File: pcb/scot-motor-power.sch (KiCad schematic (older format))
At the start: 16 parts, among them U6 TSR_1-2465, U7 INA260, U8 MCP1703A-3302_SOT223, U9 MCP1703A-5002_SOT223

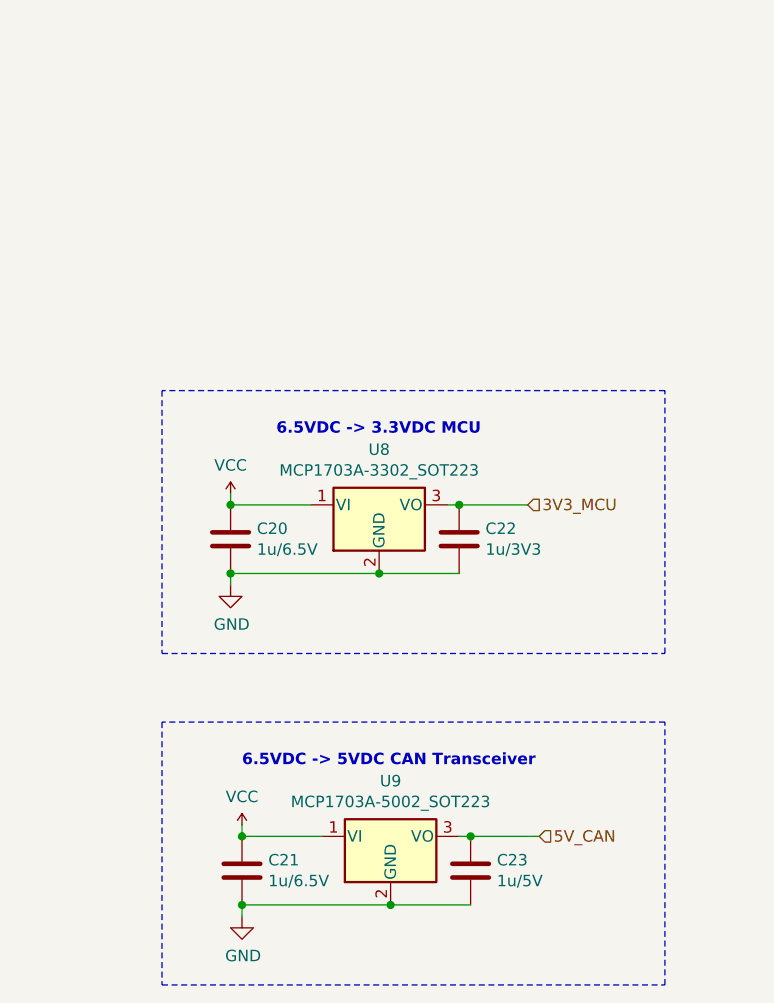
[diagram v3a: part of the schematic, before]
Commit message: pcb: Link brake clutch to e-stop, aesthetic tweaks.
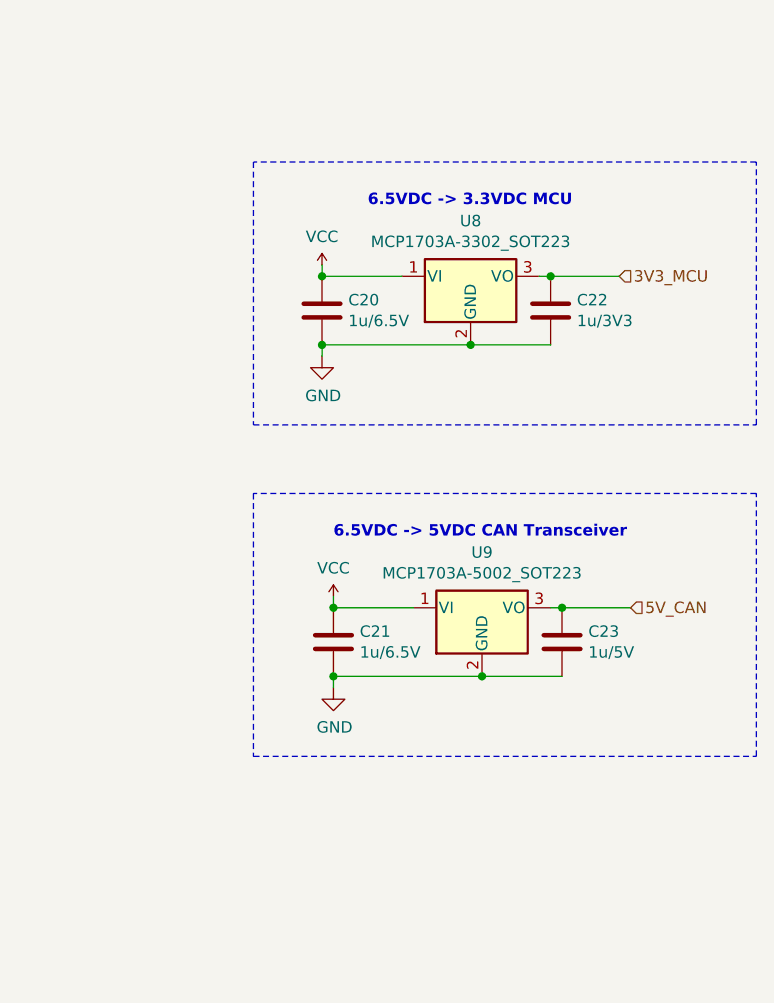
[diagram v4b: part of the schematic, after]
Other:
- moved on the sheet: C20, C21, C22, C23, U8, U9
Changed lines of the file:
@@
 L Regulator_Linear:MCP1703A-3302_SOT223 U8
 U 1 1 5F0E873C
-P 8450 4300
-F 0 "U8" H 8450 4542 50  0000 C CNN
-F 1 "MCP1703A-3302_SOT223" H 8450 4451 50  0000 C CNN
-F 2 "Package_TO_SOT_SMD:SOT-223-3_TabPin2" H 8450 4500 50  0001 C CNN
-F 3 "http://ww1.microchip.com/downloads/en/DeviceDoc/20005122B.pdf" H 8450 4250 50  0001 C CNN
-	1    8450 4300
+P 8850 3300
+F 0 "U8" H 8850 3542 50  0000 C CNN
+F 1 "MCP1703A-3302_SOT223" H 8850 3451 50  0000 C CNN
+F 2 "Package_TO_SOT_SMD:SOT-223-3_TabPin2" H 8850 3500 50  0001 C CNN
+F 3 "http://ww1.microchip.com/downloads/en/DeviceDoc/20005122B.pdf" H 8850 3250 50  0001 C CNN
+	1    8850 3300
 	1    0    0    -1
 $EndComp
@@
 L Device:C C20
 U 1 1 5F0E8CBD
-P 7800 4450
-F 0 "C20" H 7915 4496 50  0000 L CNN
-F 1 "1u/6.5V" H 7915 4405 50  0000 L CNN
-F 2 "Capacitor_SMD:C_0603_1608Metric_Pad1.05x0.95mm_HandSolder" H 7838 4300 50  0001 C CNN
-F 3 "~" H 7800 4450 50  0001 C CNN
-	1    7800 4450
-	1    0    0    -1
-$EndComp
-Wire Wire Line
-	8450 4600 7800 4600
-Wire Wire Line
-	7800 4300 8150 4300
+P 8200 3450
+F 0 "C20" H 8315 3496 50  0000 L CNN
+F 1 "1u/6.5V" H 8315 3405 50  0000 L CNN
+F 2 "Capacitor_SMD:C_0603_1608Metric_Pad1.05x0.95mm_HandSolder" H 8238 3300 50  0001 C CNN
+F 3 "~" H 8200 3450 50  0001 C CNN
+	1    8200 3450
+	1    0    0    -1
+$EndComp
+Wire Wire Line
+	8850 3600 8200 3600
+Wire Wire Line
+	8200 3300 8550 3300
 $Comp
 L Device:C C22
 U 1 1 5F0E9FCA
-P 8800 4450
-F 0 "C22" H 8915 4496 50  0000 L CNN
-F 1 "1u/3V3" H 8915 4405 50  0000 L CNN
-F 2 "Capacitor_SMD:C_0603_1608Metric_Pad1.05x0.95mm_HandSolder" H 8838 4300 50  0001 C CNN
-F 3 "~" H 8800 4450 50  0001 C CNN
-	1    8800 4450
-	1    0    0    -1
-$EndComp
-Wire Wire Line
-	8450 4600 8800 4600
-Connection ~ 8450 4600
-Wire Wire Line
-	8800 4300 8750 4300
+P 9200 3450
+F 0 "C22" H 9315 3496 50  0000 L CNN
+F 1 "1u/3V3" H 9315 3405 50  0000 L CNN
+F 2 "Capacitor_SMD:C_0603_1608Metric_Pad1.05x0.95mm_HandSolder" H 9238 3300 50  0001 C CNN
+F 3 "~" H 9200 3450 50  0001 C CNN
+	1    9200 3450
+	1    0    0    -1
+$EndComp
+Wire Wire Line
+	8850 3600 9200 3600
+Connection ~ 8850 3600
+Wire Wire Line
+	9200 3300 9150 3300
 Wire Wire Line
 	5350 5100 5200 5100
@@
 L agg-kicad:VCC #PWR0130
 U 1 1 5F0ED075
-P 7800 4250
-F 0 "#PWR0130" H 7800 4360 50  0001 L CNN
-F 1 "VCC" H 7800 4373 50  0000 C CNN
-F 2 "" H 7800 4250 50  0001 C CNN
-F 3 "" H 7800 4250 50  0001 C CNN
-	1    7800 4250
+P 8200 3250
+F 0 "#PWR0130" H 8200 3360 50  0001 L CNN
+F 1 "VCC" H 8200 3373 50  0000 C CNN
+F 2 "" H 8200 3250 50  0001 C CNN
+F 3 "" H 8200 3250 50  0001 C CNN
+	1    8200 3250
 	1    0    0    -1
 $EndComp
@@
 L power:GND #PWR0131
 U 1 1 5F0ED86E
-P 7800 4650
-F 0 "#PWR0131" H 7800 4400 50  0001 C CNN
-F 1 "GND" H 7805 4477 50  0000 C CNN
-F 2 "" H 7800 4650 50  0001 C CNN
-F 3 "" H 7800 4650 50  0001 C CNN
-	1    7800 4650
-	1    0    0    -1
-$EndComp
-Wire Wire Line
-	7800 4600 7800 4650
-Connection ~ 7800 4600
-Wire Wire Line
-	7800 4300 7800 4250
-Connection ~ 7800 4300
+P 8200 3650
+F 0 "#PWR0131" H 8200 3400 50  0001 C CNN
+F 1 "GND" H 8205 3477 50  0000 C CNN
+F 2 "" H 8200 3650 50  0001 C CNN
+F 3 "" H 8200 3650 50  0001 C CNN
+	1    8200 3650
+	1    0    0    -1
+$EndComp
+Wire Wire Line
+	8200 3600 8200 3650
+Connection ~ 8200 3600
+Wire Wire Line
+	8200 3300 8200 3250
+Connection ~ 8200 3300
 $Comp
 L agg-kicad:VCC #PWR0132
@@
 	1    0    0    -1
 $EndComp
-Text HLabel 9100 4300 2    50   Input ~ 0
+Text HLabel 9500 3300 2    50   Input ~ 0
 3V3_MCU
 Wire Wire Line
-	9100 4300 8800 4300
-Connection ~ 8800 4300
+	9500 3300 9200 3300
+Connection ~ 9200 3300
 $Comp
 L Device:C C21
 U 1 1 5F111717
-P 7850 5900
-F 0 "C21" H 7965 5946 50  0000 L CNN
-F 1 "1u/6.5V" H 7965 5855 50  0000 L CNN
-F 2 "Capacitor_SMD:C_0603_1608Metric_Pad1.05x0.95mm_HandSolder" H 7888 5750 50  0001 C CNN
-F 3 "~" H 7850 5900 50  0001 C CNN
-	1    7850 5900
-	1    0    0    -1
-$EndComp
-Wire Wire Line
-	7850 5750 8200 5750
+P 8250 4900
+F 0 "C21" H 8365 4946 50  0000 L CNN
+F 1 "1u/6.5V" H 8365 4855 50  0000 L CNN
+F 2 "Capacitor_SMD:C_0603_1608Metric_Pad1.05x0.95mm_HandSolder" H 8288 4750 50  0001 C CNN
+F 3 "~" H 8250 4900 50  0001 C CNN
+	1    8250 4900
+	1    0    0    -1
+$EndComp
+Wire Wire Line
+	8250 4750 8600 4750
 $Comp
 L Device:C C23
 U 1 1 5F111723
-P 8850 5900
-F 0 "C23" H 8965 5946 50  0000 L CNN
-F 1 "1u/5V" H 8965 5855 50  0000 L CNN
-F 2 "Capacitor_SMD:C_0603_1608Metric_Pad1.05x0.95mm_HandSolder" H 8888 5750 50  0001 C CNN
-F 3 "~" H 8850 5900 50  0001 C CNN
-	1    8850 5900
-	1    0    0    -1
-$EndComp
-Wire Wire Line
-	8850 5750 8800 5750
+P 9250 4900
+F 0 "C23" H 9365 4946 50  0000 L CNN
+F 1 "1u/5V" H 9365 4855 50  0000 L CNN
+F 2 "Capacitor_SMD:C_0603_1608Metric_Pad1.05x0.95mm_HandSolder" H 9288 4750 50  0001 C CNN
+F 3 "~" H 9250 4900 50  0001 C CNN
+	1    9250 4900
+	1    0    0    -1
+$EndComp
+Wire Wire Line
+	9250 4750 9200 4750
 $Comp
 L agg-kicad:VCC #PWR0134
 U 1 1 5F111730
-P 7850 5700
-F 0 "#PWR0134" H 7850 5810 50  0001 L CNN
-F 1 "VCC" H 7850 5823 50  0000 C CNN
-F 2 "" H 7850 5700 50  0001 C CNN
-F 3 "" H 7850 5700 50  0001 C CNN
-	1    7850 5700
+P 8250 4700
+F 0 "#PWR0134" H 8250 4810 50  0001 L CNN
+F 1 "VCC" H 8250 4823 50  0000 C CNN
+F 2 "" H 8250 4700 50  0001 C CNN
+F 3 "" H 8250 4700 50  0001 C CNN
+	1    8250 4700
 	1    0    0    -1
 $EndComp
@@
 L power:GND #PWR0135
 U 1 1 5F11173A
-P 7850 6100
-F 0 "#PWR0135" H 7850 5850 50  0001 C CNN
-F 1 "GND" H 7855 5927 50  0000 C CNN
-F 2 "" H 7850 6100 50  0001 C CNN
-F 3 "" H 7850 6100 50  0001 C CNN
-	1    7850 6100
-	1    0    0    -1
-$EndComp
-Wire Wire Line
-	7850 6050 7850 6100
-Connection ~ 7850 6050
-Wire Wire Line
-	7850 5750 7850 5700
-Connection ~ 7850 5750
-Text HLabel 9150 5750 2    50   Input ~ 0
+P 8250 5100
+F 0 "#PWR0135" H 8250 4850 50  0001 C CNN
+F 1 "GND" H 8255 4927 50  0000 C CNN
+F 2 "" H 8250 5100 50  0001 C CNN
+F 3 "" H 8250 5100 50  0001 C CNN
+	1    8250 5100
+	1    0    0    -1
+$EndComp
+Wire Wire Line
+	8250 5050 8250 5100
+Connection ~ 8250 5050
+Wire Wire Line
+	8250 4750 8250 4700
+Connection ~ 8250 4750
+Text HLabel 9550 4750 2    50   Input ~ 0
 5V_CAN
 Wire Wire Line
-	9150 5750 8850 5750
-Connection ~ 8850 5750
-Wire Wire Line
-	7850 6050 8500 6050
+	9550 4750 9250 4750
+Connection ~ 9250 4750
+Wire Wire Line
+	8250 5050 8900 5050
 $Comp
 L Regulator_Linear:MCP1703A-5002_SOT223 U9
 U 1 1 5F1147A2
-P 8500 5750
-F 0 "U9" H 8500 5992 50  0000 C CNN
-F 1 "MCP1703A-5002_SOT223" H 8500 5901 50  0000 C CNN
-F 2 "Package_TO_SOT_SMD:SOT-223-3_TabPin2" H 8500 5950 50  0001 C CNN
-F 3 "http://ww1.microchip.com/downloads/en/DeviceDoc/20005122B.pdf" H 8500 5700 50  0001 C CNN
-	1    8500 5750
-	1    0    0    -1
-$EndComp
-Connection ~ 8500 6050
-Wire Wire Line
-	8500 6050 8850 6050
+P 8900 4750
+F 0 "U9" H 8900 4992 50  0000 C CNN
+F 1 "MCP1703A-5002_SOT223" H 8900 4901 50  0000 C CNN
+F 2 "Package_TO_SOT_SMD:SOT-223-3_TabPin2" H 8900 4950 50  0001 C CNN
+F 3 "http://ww1.microchip.com/downloads/en/DeviceDoc/20005122B.pdf" H 8900 4700 50  0001 C CNN
+	1    8900 4750
+	1    0    0    -1
+$EndComp
+Connection ~ 8900 5050
+Wire Wire Line
+	8900 5050 9250 5050
 $Comp
 L Regulator_Switching:TSR_1-2465 U6
@@
 Wire Wire Line
 	5350 5400 4750 5400
-Text Notes 7850 5450 0    50   ~ 10
+Text Notes 8250 4450 0    50   ~ 10
 6.5VDC -> 5VDC CAN Transceiver
-Text Notes 8000 4000 0    50   ~ 10
+Text Notes 8400 3000 0    50   ~ 10
 6.5VDC -> 3.3VDC MCU
 Text Notes 3900 4750 0    50   ~ 10
@@
 	6750 4500 6750 5700
 Wire Notes Line
-	7500 3800 7500 4950
-Wire Notes Line
-	7500 4950 9700 4950
-Wire Notes Line
-	9700 4950 9700 3800
-Wire Notes Line
-	9700 3800 7500 3800
-Wire Notes Line
-	7500 5250 7500 6400
-Wire Notes Line
-	7500 6400 9700 6400
-Wire Notes Line
-	9700 6400 9700 5250
-Wire Notes Line
-	9700 5250 7500 5250
+	7900 2800 7900 3950
+Wire Notes Line
+	7900 3950 10100 3950
+Wire Notes Line
+	10100 3950 10100 2800
+Wire Notes Line
+	10100 2800 7900 2800
+Wire Notes Line
+	7900 4250 7900 5400
+Wire Notes Line
+	7900 5400 10100 5400
+Wire Notes Line
+	10100 5400 10100 4250
+Wire Notes Line
+	10100 4250 7900 4250
 Wire Notes Line
 	2800 2100 2800 4000

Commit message: PCB progress, schematic fixes.
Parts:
- added C25: 1u/6.5V, Capacitor_SMD:C_0603_1608Metric_Pad1.05x0.95mm_HandSolder, symbol Device:C
- added C26: 1u/3V3, Capacitor_SMD:C_0603_1608Metric_Pad1.05x0.95mm_HandSolder, symbol Device:C
- added U11: MCP1703A-3302_SOT223, Package_TO_SOT_SMD:SOT-223-3_TabPin2, symbol Regulator_Linear:MCP1703A-3302_SOT223
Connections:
- net 3V3_MCU: now also C26.1, U11.3 (VO); no longer C22.1, U8.3 (VO)
- net GND: now also C25.2, C26.2, U11.2 (GND)
- net VCC renamed 6V5_SWREG
- net 6V5_SWREG: now also C25.1, U11.1 (VI)
- new net 3V3_SWITCHES: C22.1, U8.3 (VO)
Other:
- note added: "6.5VDC -> 3.3VDC SWITCHES"
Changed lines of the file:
@@
 	3450 5100 3850 5100
-$Comp
-L agg-kicad:VCC #PWR0130
-U 1 1 5F0ED075
-P 8200 3250
-F 0 "#PWR0130" H 8200 3360 50  0001 L CNN
-F 1 "VCC" H 8200 3373 50  0000 C CNN
-F 2 "" H 8200 3250 50  0001 C CNN
-F 3 "" H 8200 3250 50  0001 C CNN
-	1    8200 3250
-	1    0    0    -1
-$EndComp
 $Comp
 L power:GND #PWR0131
@@
 Connection ~ 8200 3600
 Wire Wire Line
-	8200 3300 8200 3250
-Connection ~ 8200 3300
-$Comp
-L agg-kicad:VCC #PWR0132
-U 1 1 5F0F5376
-P 5600 5050
-F 0 "#PWR0132" H 5600 5160 50  0001 L CNN
-F 1 "VCC" H 5600 5173 50  0000 C CNN
-F 2 "" H 5600 5050 50  0001 C CNN
-F 3 "" H 5600 5050 50  0001 C CNN
-	1    5600 5050
-	1    0    0    -1
-$EndComp
-Wire Wire Line
-	5600 5050 5600 5100
-Wire Wire Line
 	5600 5100 5350 5100
 Connection ~ 5350 5100
@@
 $EndComp
 Text HLabel 9500 3300 2    50   Input ~ 0
-3V3_MCU
+3V3_SWITCHES
 Wire Wire Line
 	9500 3300 9200 3300
@@
 	9250 4750 9200 4750
 $Comp
-L agg-kicad:VCC #PWR0134
-U 1 1 5F111730
-P 8250 4700
-F 0 "#PWR0134" H 8250 4810 50  0001 L CNN
-F 1 "VCC" H 8250 4823 50  0000 C CNN
-F 2 "" H 8250 4700 50  0001 C CNN
-F 3 "" H 8250 4700 50  0001 C CNN
-	1    8250 4700
-	1    0    0    -1
-$EndComp
-$Comp
 L power:GND #PWR0135
 U 1 1 5F11173A
@@
 	8250 5050 8250 5100
 Connection ~ 8250 5050
-Wire Wire Line
-	8250 4750 8250 4700
-Connection ~ 8250 4750
 Text HLabel 9550 4750 2    50   Input ~ 0
 5V_CAN
@@
 6.5VDC -> 5VDC CAN Transceiver
 Text Notes 8400 3000 0    50   ~ 10
-6.5VDC -> 3.3VDC MCU
+6.5VDC -> 3.3VDC SWITCHES
 Text Notes 3900 4750 0    50   ~ 10
 28VDC -> 6.5VDC Power Input
@@
 	7900 2800 7900 3950
 Wire Notes Line
-	7900 3950 10100 3950
-Wire Notes Line
-	10100 3950 10100 2800
-Wire Notes Line
-	10100 2800 7900 2800
+	7900 3950 10200 3950
+Wire Notes Line
+	10200 3950 10200 2800
+Wire Notes Line
+	10200 2800 7900 2800
 Wire Notes Line
 	7900 4250 7900 5400
@@
 	4750 2500 4450 2500
 Connection ~ 4750 2500
+$Comp
+L Regulator_Linear:MCP1703A-3302_SOT223 U11
+U 1 1 5E915E90
+P 8850 1950
+F 0 "U11" H 8850 2192 50  0000 C CNN
+F 1 "MCP1703A-3302_SOT223" H 8850 2101 50  0000 C CNN
+F 2 "Package_TO_SOT_SMD:SOT-223-3_TabPin2" H 8850 2150 50  0001 C CNN
+F 3 "http://ww1.microchip.com/downloads/en/DeviceDoc/20005122B.pdf" H 8850 1900 50  0001 C CNN
+	1    8850 1950
+	1    0    0    -1
+$EndComp
+$Comp
+L Device:C C25
+U 1 1 5E915E9A
+P 8200 2100
+F 0 "C25" H 8315 2146 50  0000 L CNN
+F 1 "1u/6.5V" H 8315 2055 50  0000 L CNN
+F 2 "Capacitor_SMD:C_0603_1608Metric_Pad1.05x0.95mm_HandSolder" H 8238 1950 50  0001 C CNN
+F 3 "~" H 8200 2100 50  0001 C CNN
+	1    8200 2100
+	1    0    0    -1
+$EndComp
+Wire Wire Line
+	8850 2250 8200 2250
+Wire Wire Line
+	8200 1950 8550 1950
+$Comp
+L Device:C C26
+U 1 1 5E915EA6
+P 9200 2100
+F 0 "C26" H 9315 2146 50  0000 L CNN
+F 1 "1u/3V3" H 9315 2055 50  0000 L CNN
+F 2 "Capacitor_SMD:C_0603_1608Metric_Pad1.05x0.95mm_HandSolder" H 9238 1950 50  0001 C CNN
+F 3 "~" H 9200 2100 50  0001 C CNN
+	1    9200 2100
+	1    0    0    -1
+$EndComp
+Wire Wire Line
+	8850 2250 9200 2250
+Connection ~ 8850 2250
+Wire Wire Line
+	9200 1950 9150 1950
+$Comp
+L power:GND #PWR0119
+U 1 1 5E915EBD
+P 8200 2300
+F 0 "#PWR0119" H 8200 2050 50  0001 C CNN
+F 1 "GND" H 8205 2127 50  0000 C CNN
+F 2 "" H 8200 2300 50  0001 C CNN
+F 3 "" H 8200 2300 50  0001 C CNN
+	1    8200 2300
+	1    0    0    -1
+$EndComp
+Wire Wire Line
+	8200 2250 8200 2300
+Connection ~ 8200 2250
+Text HLabel 9500 1950 2    50   Input ~ 0
+3V3_MCU
+Wire Wire Line
+	9500 1950 9200 1950
+Connection ~ 9200 1950
+Text Notes 8400 1650 0    50   ~ 10
+6.5VDC -> 3.3VDC MCU
+Wire Notes Line
+	7900 1450 7900 2600
+Wire Notes Line
+	7900 2600 10100 2600
+Wire Notes Line
+	10100 2600 10100 1450
+Wire Notes Line
+	10100 1450 7900 1450
+Wire Wire Line
+	5600 4700 6100 4700
+Wire Wire Line
+	5600 4700 5600 5100
+Text Label 8600 4750 2    50   ~ 0
+6V5_SWREG
+Text Label 8550 3300 2    50   ~ 0
+6V5_SWREG
+Text Label 8550 1950 2    50   ~ 0
+6V5_SWREG
+Text Label 6100 4700 2    50   ~ 0
+6V5_SWREG
 $EndSCHEMATC

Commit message: PCB progress.
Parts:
- removed R18: 1K, Resistor_SMD:R_0603_1608Metric_Pad1.05x0.95mm_HandSolder, symbol Device:R
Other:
- moved on the sheet: C16
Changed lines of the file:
@@
 Wire Wire Line
 	4350 2500 3750 2500
-Text HLabel 3400 3050 0    50   Input ~ 0
+Text HLabel 3650 2950 0    50   Input ~ 0
 3V3_MCU
 $Comp
 L Device:C C16
 U 1 1 5F123658
-P 3450 3200
-F 0 "C16" H 3565 3246 50  0000 L CNN
-F 1 "100n/3V3" H 3565 3155 50  0000 L CNN
-F 2 "Capacitor_SMD:C_0603_1608Metric_Pad1.05x0.95mm_HandSolder" H 3488 3050 50  0001 C CNN
-F 3 "~" H 3450 3200 50  0001 C CNN
-	1    3450 3200
-	1    0    0    -1
-$EndComp
-$Comp
-L Device:R R18
-U 1 1 5F1256CC
-P 4050 3200
-F 0 "R18" H 3980 3154 50  0000 R CNN
-F 1 "1K" H 3980 3245 50  0000 R CNN
-F 2 "Resistor_SMD:R_0603_1608Metric_Pad1.05x0.95mm_HandSolder" V 3980 3200 50  0001 C CNN
-F 3 "~" H 4050 3200 50  0001 C CNN
-	1    4050 3200
-	-1   0    0    1
-$EndComp
-Wire Wire Line
-	4050 3050 4050 2950
-Wire Wire Line
-	4050 2950 4150 2950
-Wire Wire Line
-	4050 3350 4050 3400
-Wire Wire Line
-	4050 3400 4350 3400
-Wire Wire Line
-	4350 3400 4350 3350
-Wire Wire Line
-	4050 3050 3450 3050
-Connection ~ 4050 3050
-Connection ~ 3450 3050
-Wire Wire Line
-	3450 3050 3400 3050
+P 3700 3100
+F 0 "C16" H 3815 3146 50  0000 L CNN
+F 1 "100n/3V3" H 3815 3055 50  0000 L CNN
+F 2 "Capacitor_SMD:C_0603_1608Metric_Pad1.05x0.95mm_HandSolder" H 3738 2950 50  0001 C CNN
+F 3 "~" H 3700 3100 50  0001 C CNN
+	1    3700 3100
+	1    0    0    -1
+$EndComp
+Connection ~ 3700 2950
+Wire Wire Line
+	3700 2950 3650 2950
 $Comp
 L power:GND #PWR0137
 U 1 1 5F129CB1
-P 3450 3350
-F 0 "#PWR0137" H 3450 3100 50  0001 C CNN
-F 1 "GND" H 3455 3177 50  0000 C CNN
-F 2 "" H 3450 3350 50  0001 C CNN
-F 3 "" H 3450 3350 50  0001 C CNN
-	1    3450 3350
+P 3700 3250
+F 0 "#PWR0137" H 3700 3000 50  0001 C CNN
+F 1 "GND" H 3705 3077 50  0000 C CNN
+F 2 "" H 3700 3250 50  0001 C CNN
+F 3 "" H 3700 3250 50  0001 C CNN
+	1    3700 3250
 	1    0    0    -1
 $EndComp
@@
 	4450 3700 4800 3700
 Wire Wire Line
-	4350 3400 4350 3800
-Wire Wire Line
 	4350 3800 4800 3800
-Connection ~ 4350 3400
 Text HLabel 4800 3600 2    50   Input ~ 0
 VI_SDA
@@
 Text Label 6100 4700 2    50   ~ 0
 6V5_SWREG
+Wire Wire Line
+	4350 3350 4350 3800
+Wire Wire Line
+	3700 2950 4150 2950
 $EndSCHEMATC

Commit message: PCB Progress.
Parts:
- C17: value 2u2/35V -> 4u7/50V; footprint Capacitor_SMD:C_0603_1608Metric_Pad1.05x0.95mm_HandSolder -> Capacitor_SMD:C_1206_3216Metric_Pad1.42x1.75mm_HandSolder
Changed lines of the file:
@@
 P 3450 5250
 F 0 "C17" H 3565 5296 50  0000 L CNN
-F 1 "2u2/35V" H 3565 5205 50  0000 L CNN
-F 2 "Capacitor_SMD:C_0603_1608Metric_Pad1.05x0.95mm_HandSolder" H 3488 5100 50  0001 C CNN
+F 1 "4u7/50V" H 3565 5205 50  0000 L CNN
+F 2 "Capacitor_SMD:C_1206_3216Metric_Pad1.42x1.75mm_HandSolder" H 3488 5100 50  0001 C CNN
 F 3 "~" H 3450 5250 50  0001 C CNN
 	1    3450 5250

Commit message: pcb: Final tweaks.
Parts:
- C18: value 1u/6.5V -> 4u7/6.5V; footprint Capacitor_SMD:C_0603_1608Metric_Pad1.05x0.95mm_HandSolder -> Capacitor_SMD:C_0805_2012Metric_Pad1.15x1.40mm_HandSolder
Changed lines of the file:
@@
 P 4750 5250
 F 0 "C18" H 4865 5296 50  0000 L CNN
-F 1 "1u/6.5V" H 4865 5205 50  0000 L CNN
-F 2 "Capacitor_SMD:C_0603_1608Metric_Pad1.05x0.95mm_HandSolder" H 4788 5100 50  0001 C CNN
+F 1 "4u7/6.5V" H 4865 5205 50  0000 L CNN
+F 2 "Capacitor_SMD:C_0805_2012Metric_Pad1.15x1.40mm_HandSolder" H 4788 5100 50  0001 C CNN
 F 3 "~" H 4750 5250 50  0001 C CNN
 	1    4750 5250
